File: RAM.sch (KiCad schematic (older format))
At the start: 27 parts, among them IC1 EP4CE10F17, U22 W9751G6KB

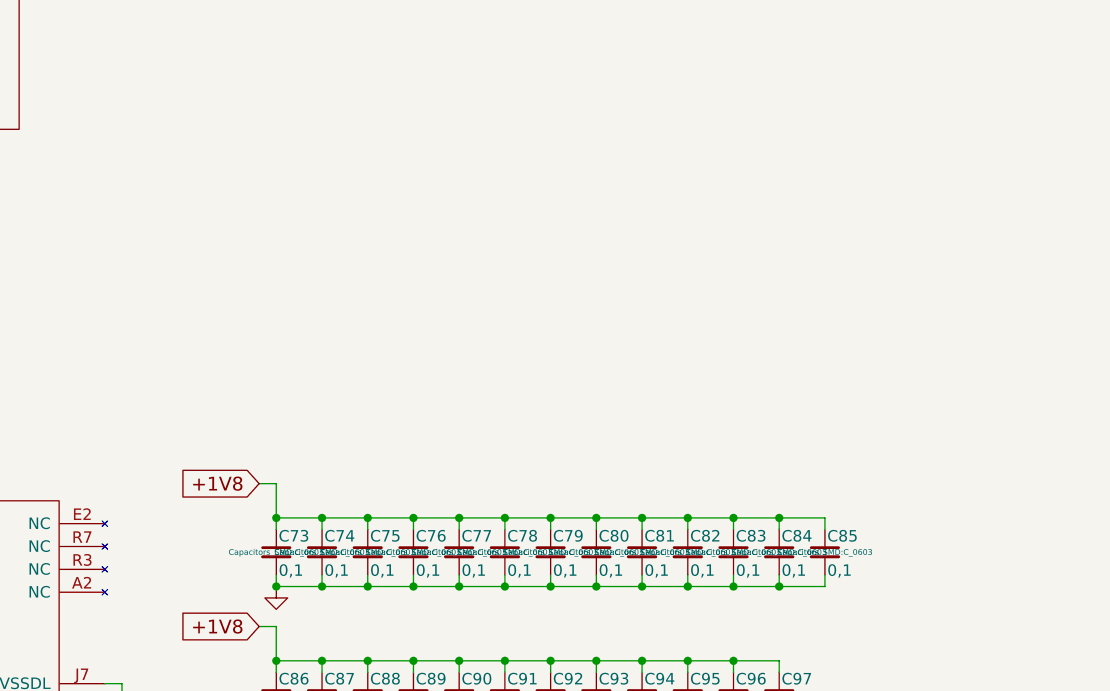
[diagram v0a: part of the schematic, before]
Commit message: 1V8 caps added, bit of routing
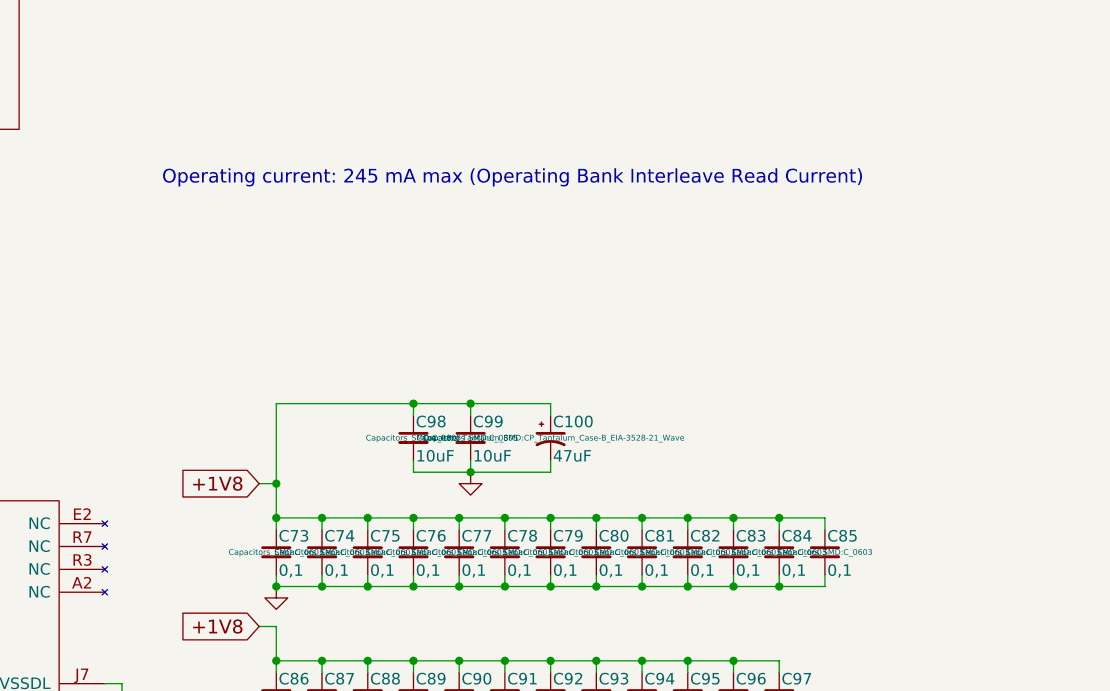
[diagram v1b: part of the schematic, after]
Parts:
- added C100: 47uF, Capacitors_Tantalum_SMD:CP_Tantalum_Case-B_EIA-3528-21_Wave, symbol CP1_Small
- added C98, C99: 10uF, Capacitors_SMD:C_0805, symbol C_Small
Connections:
- wire segments 157 -> 165
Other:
- note added: "Operating current: 245 mA max (Operating Bank Interleave Read Current)"
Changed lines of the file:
@@
 BA1
 $Comp
-L GND #PWR0131
+L GND #PWR131
 U 1 1 5882F59D
 P 6275 7300
-F 0 "#PWR0131" H 6275 7050 50  0001 C CNN
+F 0 "#PWR131" H 6275 7050 50  0001 C CNN
 F 1 "GND" H 6275 7150 50  0001 C CNN
 F 2 "" H 6275 7300 50  0000 C CNN
@@
 +1V8
 $Comp
-L GND #PWR0132
+L GND #PWR132
 U 1 1 5883C563
 P 6950 5300
-F 0 "#PWR0132" H 6950 5050 50  0001 C CNN
+F 0 "#PWR132" H 6950 5050 50  0001 C CNN
 F 1 "GND" H 6950 5150 50  0001 C CNN
 F 2 "" H 6950 5300 50  0000 C CNN
@@
 $EndComp
 $Comp
-L GND #PWR0133
+L GND #PWR133
 U 1 1 5883EF35
 P 6950 5925
-F 0 "#PWR0133" H 6950 5675 50  0001 C CNN
+F 0 "#PWR133" H 6950 5675 50  0001 C CNN
 F 1 "GND" H 6950 5775 50  0001 C CNN
 F 2 "" H 6950 5925 50  0000 C CNN
@@
 	6875 4850 6950 4850
 Wire Wire Line
-	6950 4850 6950 5050
+	6950 4500 6950 5050
 Connection ~ 6950 5000
 Connection ~ 6950 5300
@@
 Text Label 6625 1700 2    50   ~ 0
 A11
+$Comp
+L C_Small C98
+U 1 1 588A6D45
+P 7550 4650
+F 0 "C98" H 7560 4720 50  0000 L CNN
+F 1 "10uF" H 7560 4570 50  0000 L CNN
+F 2 "Capacitors_SMD:C_0805" H 7550 4650 25  0000 C CNN
+F 3 "" H 7550 4650 50  0000 C CNN
+	1    7550 4650
+	1    0    0    -1
+$EndComp
+$Comp
+L C_Small C99
+U 1 1 588A6DFE
+P 7800 4650
+F 0 "C99" H 7810 4720 50  0000 L CNN
+F 1 "10uF" H 7810 4570 50  0000 L CNN
+F 2 "Capacitors_SMD:C_0805" H 7800 4650 25  0000 C CNN
+F 3 "" H 7800 4650 50  0000 C CNN
+	1    7800 4650
+	1    0    0    -1
+$EndComp
+$Comp
+L CP1_Small C100
+U 1 1 588A704D
+P 8150 4650
+F 0 "C100" H 8160 4720 50  0000 L CNN
+F 1 "47uF" H 8160 4570 50  0000 L CNN
+F 2 "Capacitors_Tantalum_SMD:CP_Tantalum_Case-B_EIA-3528-21_Wave" H 8150 4650 25  0000 C CNN
+F 3 "" H 8150 4650 50  0000 C CNN
+	1    8150 4650
+	1    0    0    -1
+$EndComp
+Wire Wire Line
+	7550 4800 8150 4800
+Wire Wire Line
+	7800 4800 7800 4750
+Wire Wire Line
+	7550 4800 7550 4750
+Wire Wire Line
+	6950 4500 8150 4500
+Connection ~ 7800 4800
+Wire Wire Line
+	7550 4550 7550 4500
+Connection ~ 7550 4500
+Wire Wire Line
+	8150 4500 8150 4550
+Wire Wire Line
+	8150 4800 8150 4750
+Wire Wire Line
+	7800 4550 7800 4500
+Connection ~ 7800 4500
+Connection ~ 6950 4850
+$Comp
+L GND #PWR134
+U 1 1 588A8459
+P 7800 4800
+F 0 "#PWR134" H 7800 4550 50  0001 C CNN
+F 1 "GND" H 7800 4650 50  0001 C CNN
+F 2 "" H 7800 4800 50  0000 C CNN
+F 3 "" H 7800 4800 50  0000 C CNN
+	1    7800 4800
+	1    0    0    -1
+$EndComp
+Text Notes 6450 3550 0    60   ~ 0
+Operating current: 245 mA max (Operating Bank Interleave Read Current)
 $EndSCHEMATC

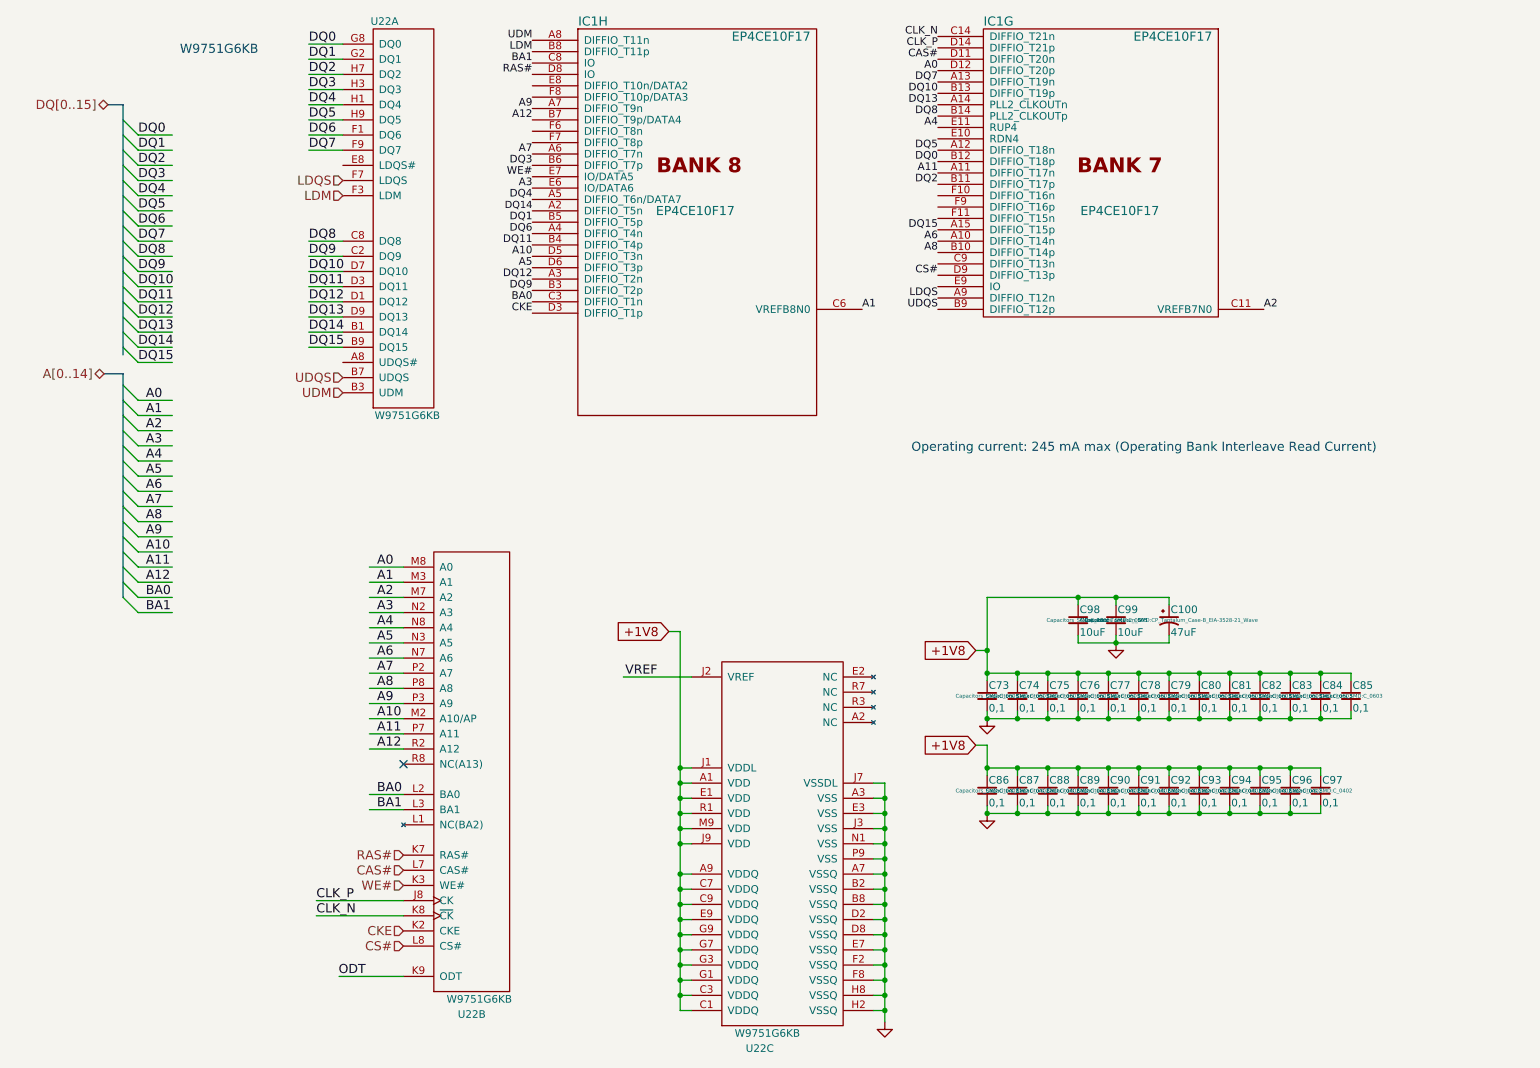
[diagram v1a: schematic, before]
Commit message: Added power sheet, 1V8 chip docs etc
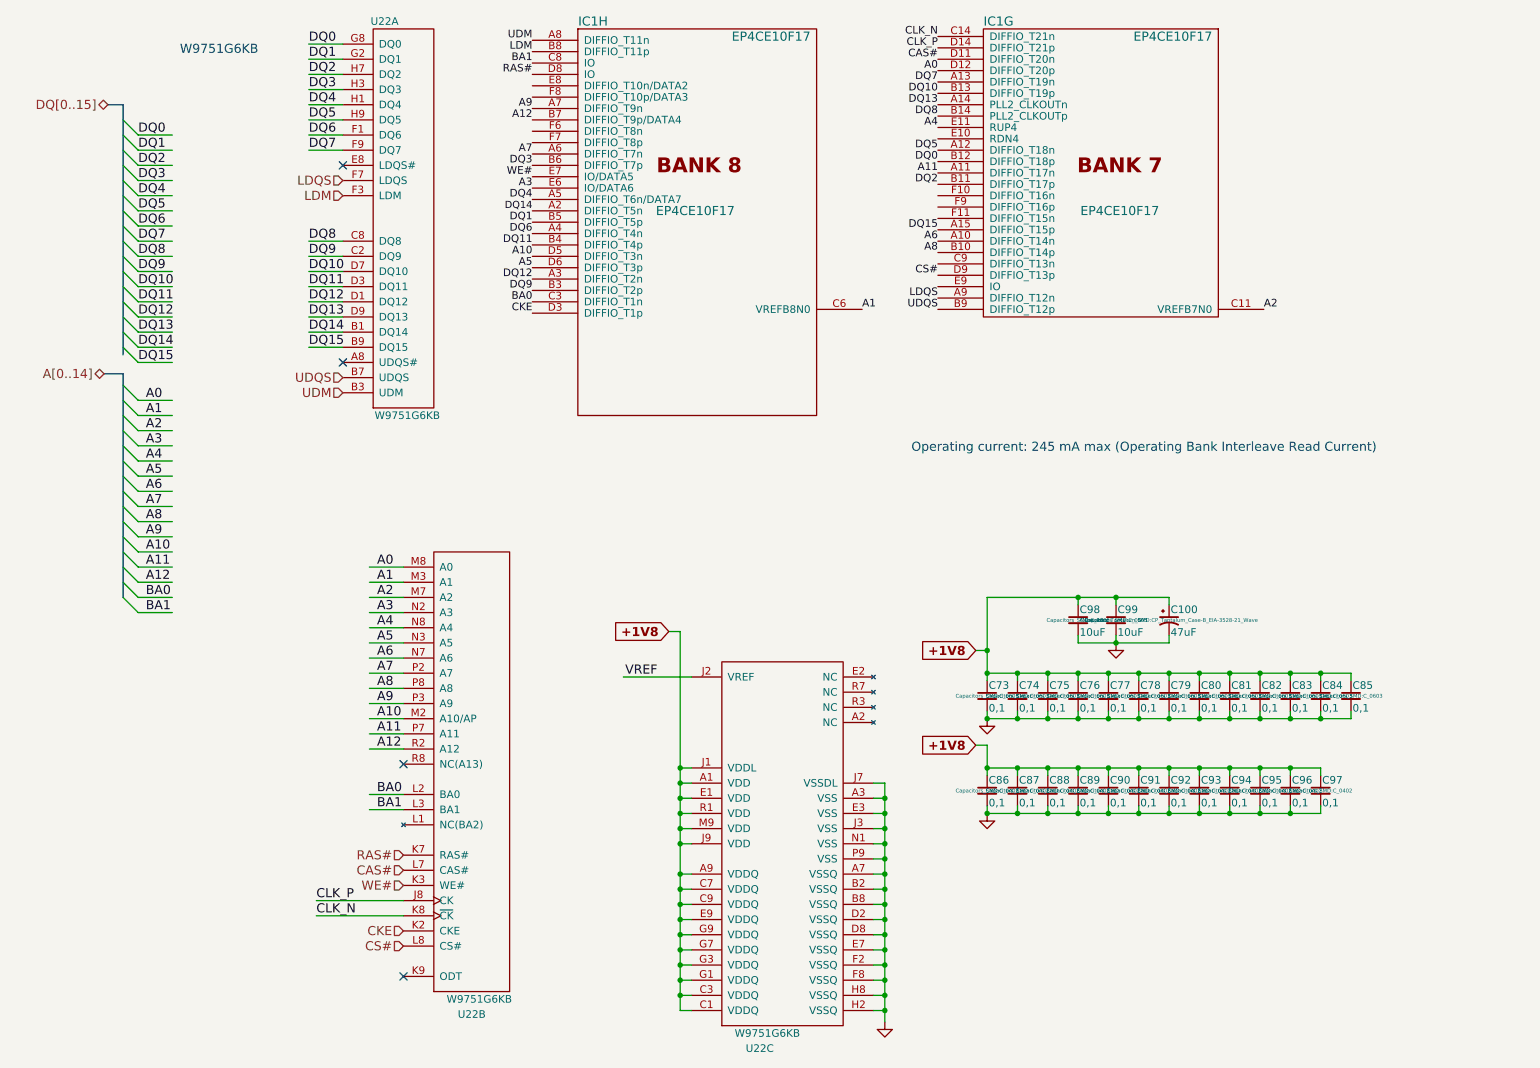
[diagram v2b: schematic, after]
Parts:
- IC1: footprint 256FBGA -> lib:BGA-256-NSMD
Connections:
- net labels removed: ODT
- wire segments 165 -> 164
- no-connect marks 1 -> 4
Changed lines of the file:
@@
 $Descr A4 11693 8268
 encoding utf-8
-Sheet 5 6
+Sheet 5 7
 Title ""
 Date ""
@@
 Text Label 1400 4600 0    60   ~ 0
 BA1
-Text Label 2850 7000 2    60   ~ 0
-ODT
 Text Label 4775 5025 2    60   ~ 0
 VREF
@@
 F 0 "IC1" H 7025 3200 60  0000 C CNN
 F 1 "EP4CE10F17" H 7825 1950 60  0000 C CNN
-F 2 "256FBGA" H 7825 3525 60  0001 C CNN
+F 2 "lib:BGA-256-NSMD" H 7825 3525 60  0001 C CNN
 F 3 "" H 5725 -100 60  0000 C CNN
 F 4 "EP4CE10F17" H 8175 3100 60  0000 C CNN "Component Value"
@@
 BA1
 $Comp
-L GND #PWR131
+L GND #PWR134
 U 1 1 5882F59D
 P 6275 7300
-F 0 "#PWR131" H 6275 7050 50  0001 C CNN
+F 0 "#PWR134" H 6275 7050 50  0001 C CNN
 F 1 "GND" H 6275 7150 50  0001 C CNN
 F 2 "" H 6275 7300 50  0000 C CNN
@@
 	1    0    0    -1
 $EndComp
-Text GLabel 4850 4725 0    60   Input ~ 0
+Text GLabel 4850 4725 0    60   Input ~ 12
 +1V8
 Text Label 6625 2075 2    50   ~ 0
@@
 	1    0    0    -1
 $EndComp
-Text GLabel 6875 4850 0    60   Input ~ 0
+Text GLabel 6875 4850 0    60   Input ~ 12
 +1V8
 $Comp
@@
 	1    0    0    -1
 $EndComp
-Text GLabel 6875 5475 0    60   Input ~ 0
+Text GLabel 6875 5475 0    60   Input ~ 12
 +1V8
 $Comp
@@
 Wire Wire Line
 	5000 5025 4550 5025
-Wire Wire Line
-	3100 7000 2675 7000
 Wire Wire Line
 	3100 6500 2525 6500
@@
 Connection ~ 6950 4850
 $Comp
-L GND #PWR134
+L GND #PWR131
 U 1 1 588A8459
 P 7800 4800
-F 0 "#PWR134" H 7800 4550 50  0001 C CNN
+F 0 "#PWR131" H 7800 4550 50  0001 C CNN
 F 1 "GND" H 7800 4650 50  0001 C CNN
 F 2 "" H 7800 4800 50  0000 C CNN
@@
 Text Notes 6450 3550 0    60   ~ 0
 Operating current: 245 mA max (Operating Bank Interleave Read Current)
+NoConn ~ 2700 2950
+NoConn ~ 2700 1650
+NoConn ~ 3100 7000
 $EndSCHEMATC

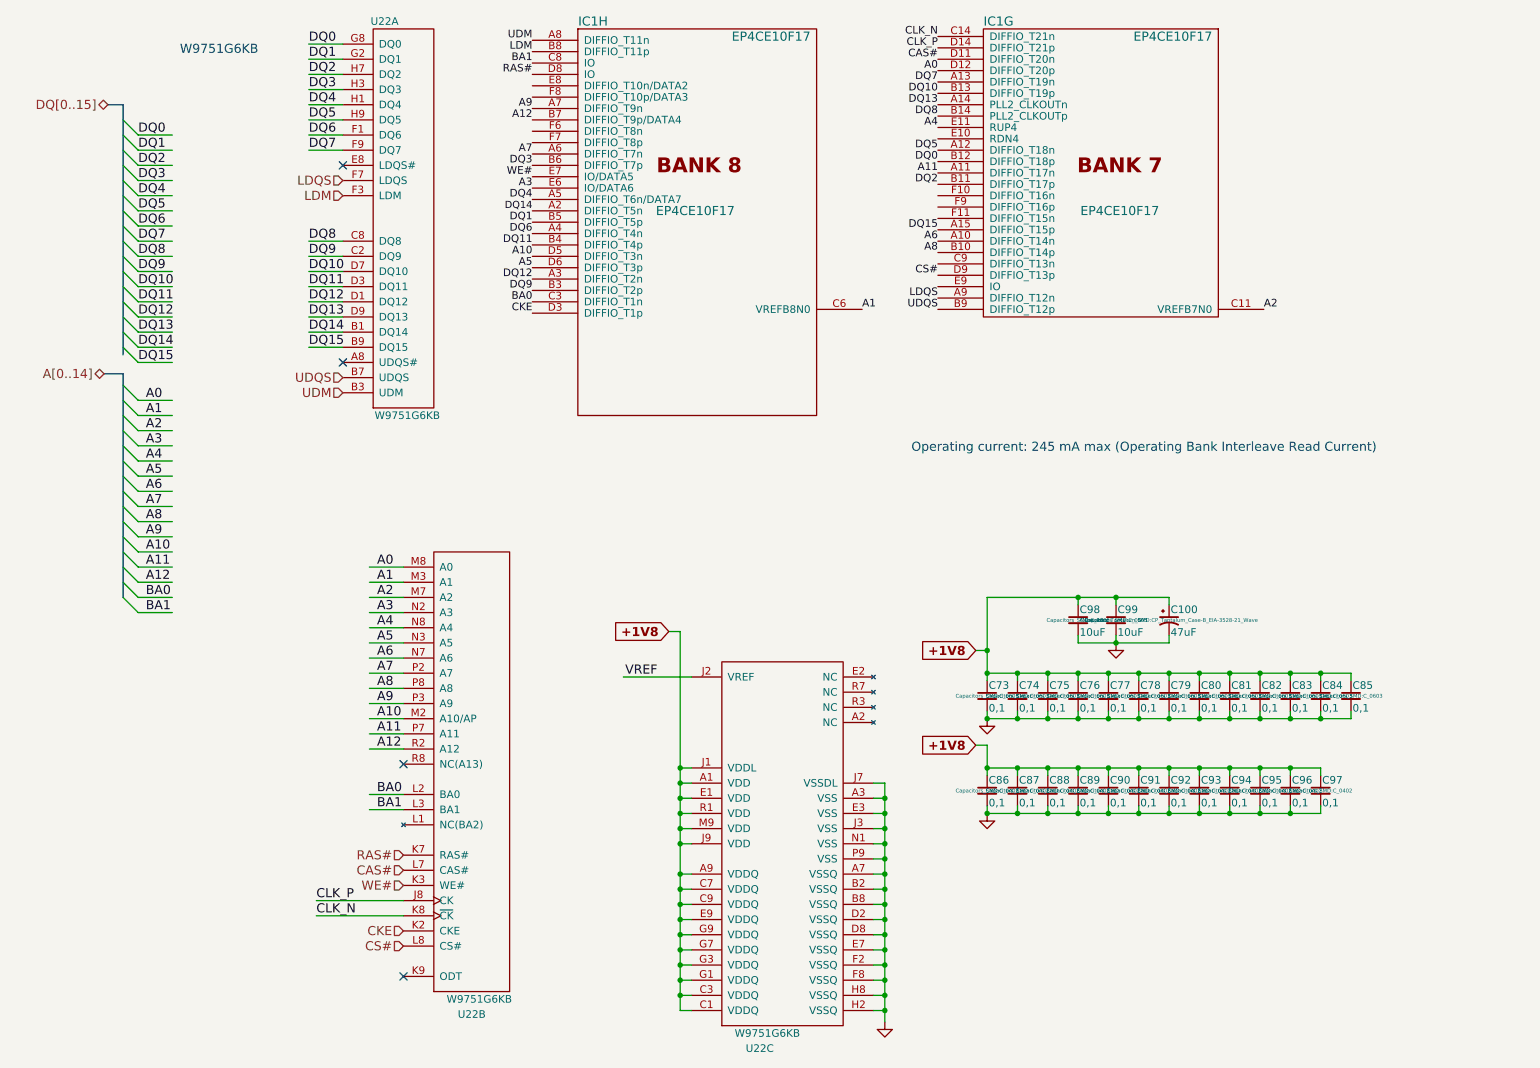
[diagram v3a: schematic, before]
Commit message: VREF for DDR2
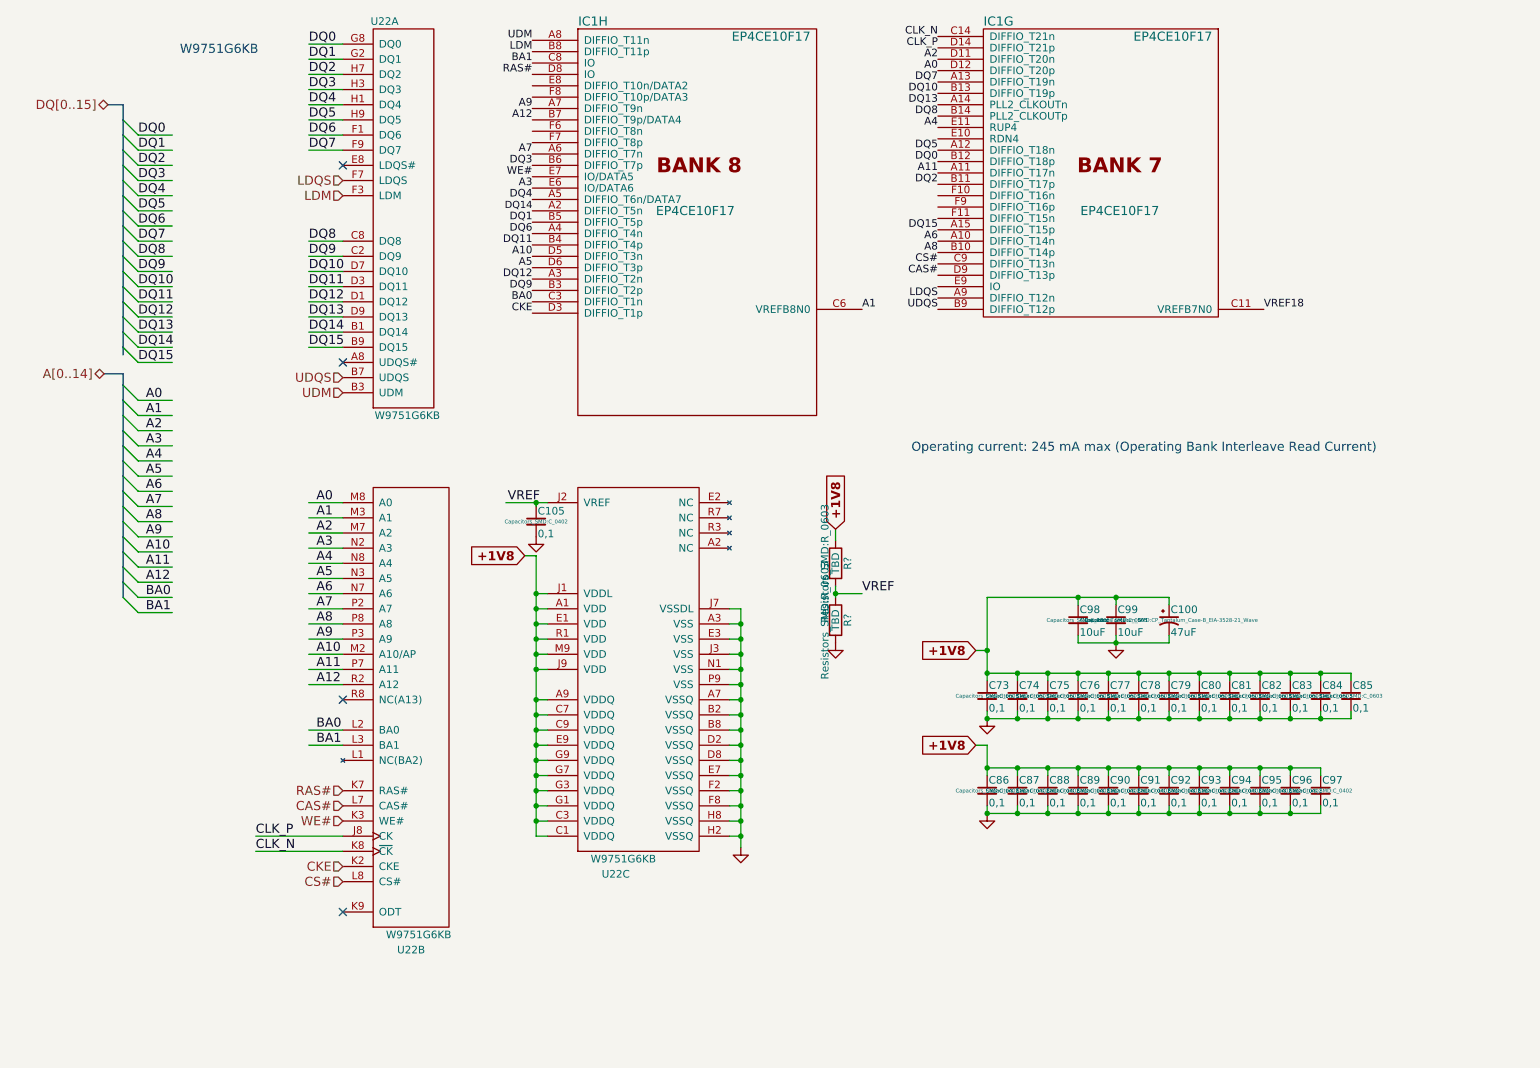
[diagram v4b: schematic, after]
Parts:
- added C105: 0,1, Capacitors_SMD:C_0402, symbol C_Small
- added R? (x2): TBD, Resistors_SMD:R_0603, symbol R
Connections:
- net labels added: VREF18
- wire segments 164 -> 248
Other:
- moved on the sheet: U22B, U22C

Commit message: VREF18 for FPGA WIP
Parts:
- gave numbers to parts that had none: 2
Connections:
- wire segments 248 -> 168
